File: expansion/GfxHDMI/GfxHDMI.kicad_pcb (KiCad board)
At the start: 4 copper layers, 100 x 100 mm, 76 parts, among them J1 JTAG, J101 D68K_64PIN_BOARD, J501 VGA Out, U101 74LS125, U102 LD1117S12TR_SOT223, U201 SN74LVC8T245PWR, U202 SN74LVC8T245PWR, U203 SN74LVC8T245PWR, U204 SN74LVC8T245PWR, U205 SN74LVC8T245PWR, U206 SN74LVC8T245PWR, U301 XC3S500E-4PQG208I, U302 W25Q64JVSSIM, U401 IS61WV102416FBLL-10TLI, U402 IS61WV102416FBLL-10TLI, U501 ADV7123JSTZ240, Y1 ECS-3963

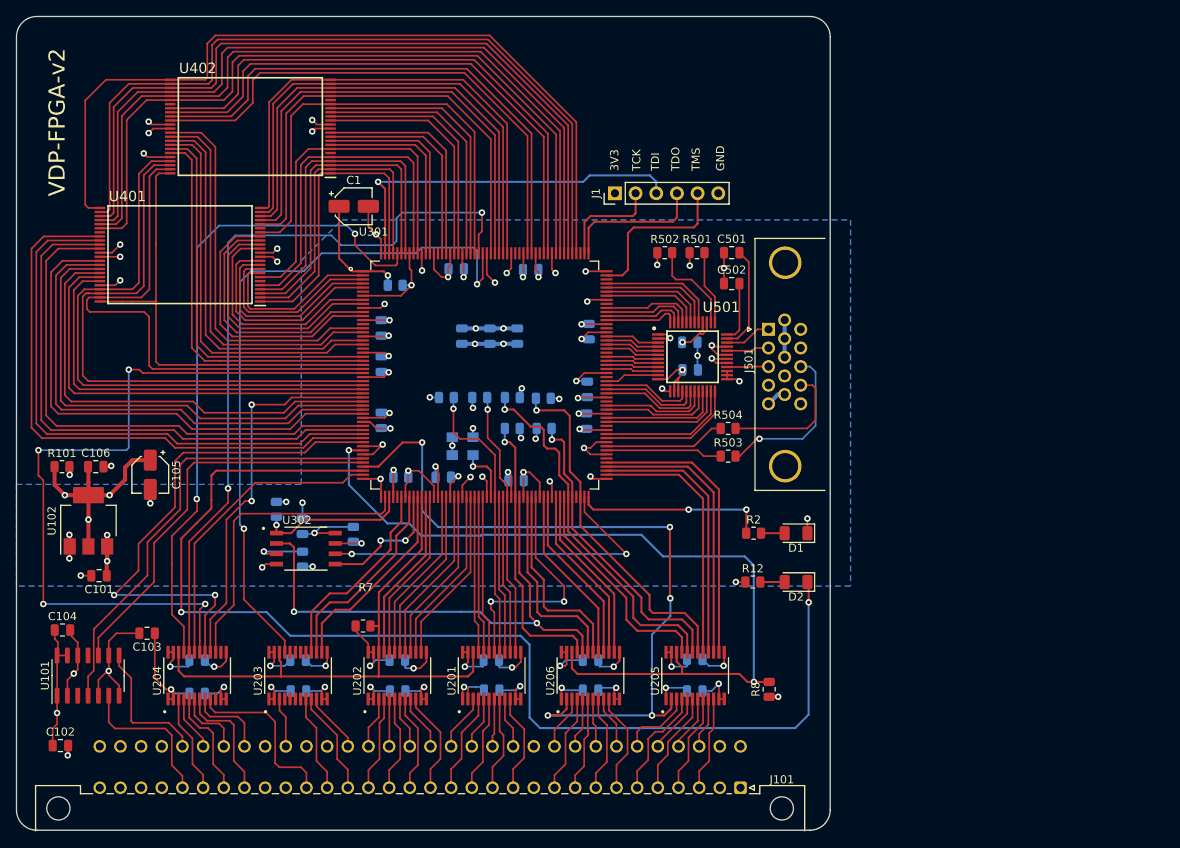
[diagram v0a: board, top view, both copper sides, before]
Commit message: Working on HDMI board
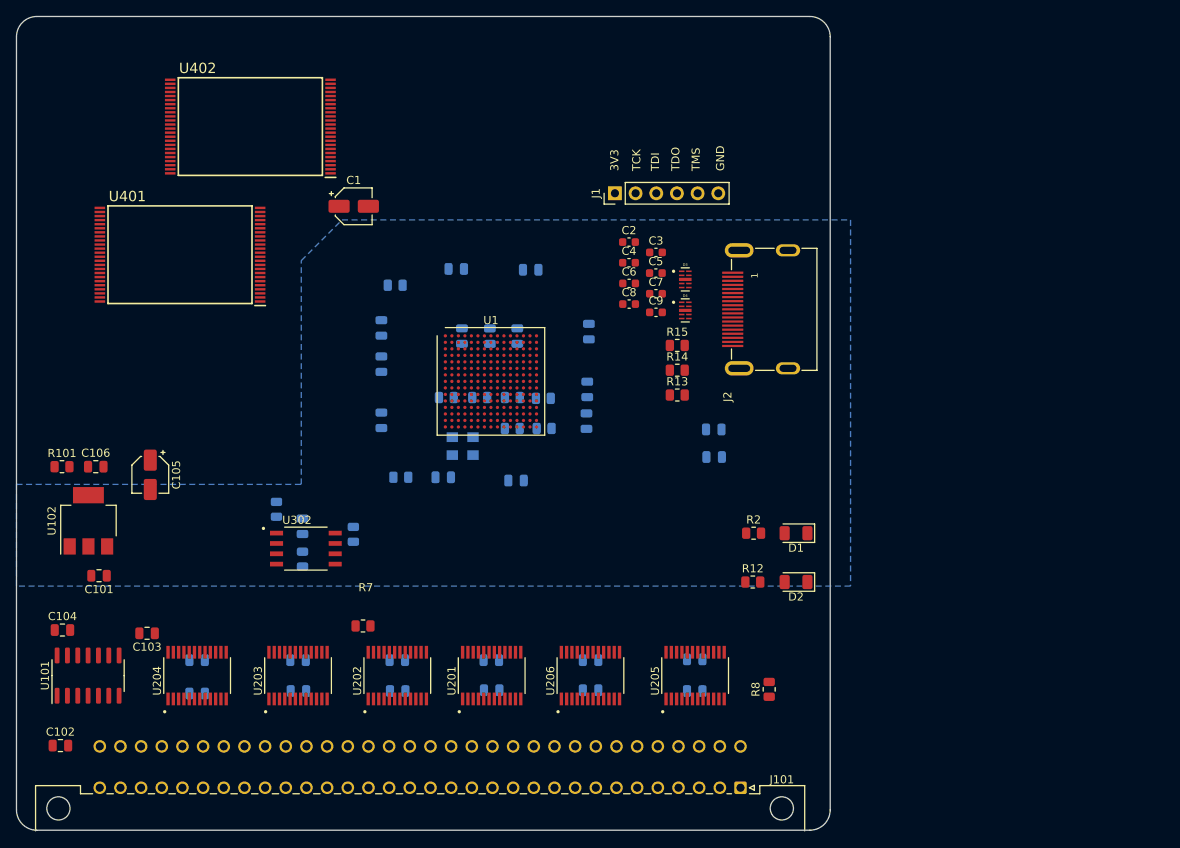
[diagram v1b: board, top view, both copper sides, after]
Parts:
- removed C501, C502: 100nF, Capacitor_SMD:C_0805_2012Metric
- removed J501: VGA Out, Connector_Dsub:DSUB-15-HD_Female_Horizontal_P2.29x1.98mm_EdgePinOffset3.03mm_Housed_MountingHolesOffset4.94mm
- removed R501: 530R, Resistor_SMD:R_0805_2012Metric
- removed R502: 10K, Resistor_SMD:R_0805_2012Metric
- removed R503, R504: 82.5R, Resistor_SMD:R_0805_2012Metric
- removed U301: XC3S500E-4PQG208I, Ddraig:QFP50P3060X3060X409-208N
- removed U501: ADV7123JSTZ240, Ddraig:QFP50P900X900X160-48N
- added C2: 100nF, Capacitor_SMD:C_0603_1608Metric, F.Cu at (175.3, 77.7)
- added C3: 100nF, Capacitor_SMD:C_0603_1608Metric, F.Cu at (178.6, 79.0)
- added C4: 100nF, Capacitor_SMD:C_0603_1608Metric, F.Cu at (175.3, 80.3)
- added C5: 100nF, Capacitor_SMD:C_0603_1608Metric, F.Cu at (178.6, 81.5)
- added C6: 100nF, Capacitor_SMD:C_0603_1608Metric, F.Cu at (175.3, 82.8)
- added C7: 100nF, Capacitor_SMD:C_0603_1608Metric, F.Cu at (178.6, 84.1)
- added C8: 100nF, Capacitor_SMD:C_0603_1608Metric, F.Cu at (175.3, 85.3)
- added C9: 100nF, Capacitor_SMD:C_0603_1608Metric, F.Cu at (178.6, 86.4)
- added D3: RCLAMP0524PATCT, Ddraig:DIO_RCLAMP0524PATCT, F.Cu at (182.2, 82.3)
- added D4: RCLAMP0524PATCT, Ddraig:DIO_RCLAMP0524PATCT, F.Cu at (182.2, 86.1)
- added J2: 685119134923, Ddraig:685119134923, F.Cu at (188.0, 86.0)
- added R13: 10K, Resistor_SMD:R_0805_2012Metric, F.Cu at (181.2, 96.5)
- added R14: 10K, Resistor_SMD:R_0805_2012Metric, F.Cu at (181.2, 93.5)
- added R15: 10K, Resistor_SMD:R_0805_2012Metric, F.Cu at (181.2, 90.4)
- added U1: XC7S25-CSGA225, Package_BGA:Xilinx_CSGA225, F.Cu at (158.3, 94.8)
- U302: value W25Q64JVSSIM -> IS25LP064D-JBLE
- moved C503 11.1 mm to (185.7, 100.8)
- moved C504 11.1 mm to (185.7, 104.1)
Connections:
- C307 pad 2: GND -> Net-(C307-Pad2)
- C308 pad 2: GND -> Net-(C307-Pad2)
- C309 pad 2: GND -> Net-(C307-Pad2)
- C310 pad 2: GND -> Net-(C307-Pad2)
- J1 pad 2: Net-(J1-Pad2) -> unconnected-(J1-Pin_2-Pad2)
- J1 pad 3: Net-(J1-Pad3) -> unconnected-(J1-Pin_3-Pad3)
- J1 pad 4: Net-(J1-Pad4) -> unconnected-(J1-Pin_4-Pad4)
- J1 pad 5: Net-(J1-Pad5) -> unconnected-(J1-Pin_5-Pad5)
- U302 pad 2: /FPGA/D14 -> /FPGA/FLASH_DO
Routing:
- net GND: track 230.9 -> 0.00 mm, vias 61 -> 0
- net +3V3: track 170.2 -> 0.00 mm, vias 42 -> 0
- net /FPGA/~{ACCESS_LED}: track 142.5 -> 0.00 mm, vias 2 -> 0
- net /FPGA/~{CPU_DATAEN}: track 104.1 -> 0.00 mm, vias 2 -> 0
- net /FPGA/SRAM_A14: track 101.4 -> 0.00 mm
- net /FPGA/SRAM_A13: track 97.3 -> 0.00 mm
- net /FPGA/SRAM_A12: track 96.3 -> 0.00 mm
- net /FPGA/SRAM_A11: track 95.1 -> 0.00 mm
- net /FPGA/~{RESET}: track 95.0 -> 0.00 mm, vias 4 -> 0
- net /FPGA/SRAM_A10: track 93.9 -> 0.00 mm
- net /FPGA/SRAM_A9: track 93.0 -> 0.00 mm
- net /FPGA/~{DATACS}: track 92.8 -> 0.00 mm, vias 2 -> 0
- net /FPGA/DATA_DIR: track 92.8 -> 0.00 mm, vias 5 -> 0
- net /FPGA/HOST_CLK: track 87.0 -> 0.00 mm, vias 2 -> 0
- net /FPGA/~{REGCS}: track 81.6 -> 0.00 mm, vias 2 -> 0
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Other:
- board text removed: "VDP-FPGA-v2"

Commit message: More work on the HDMI board
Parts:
- R13: value 10K -> 27K
- R14, R15: value 10K -> 1K5
- moved C305 62.4 mm to (220.6, 89.0)
- moved C307 62.4 mm to (225.6, 80.8)
- moved C310 62.4 mm to (214.9, 106.3)
- moved R9 62.4 mm to (223.4, 96.5)
- moved C301 62.4 mm to (224.0, 89.0)
- moved C302 62.4 mm to (232.6, 95.5)
- moved C303 62.4 mm to (217.2, 89.0)
- moved C304 62.4 mm to (207.3, 99.3)
- moved C306 62.4 mm to (232.8, 88.4)
- moved C308 62.4 mm to (232.5, 99.4)
- moved C309 62.4 mm to (207.3, 88.0)
- moved C401 62.4 mm to (223.8, 106.7)
- moved C402 62.4 mm to (207.3, 92.4)
- moved C404 62.4 mm to (216.5, 80.7)
- moved R1 62.4 mm to (219.4, 96.5)
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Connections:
- C307 pad 2: Net-(C307-Pad2) -> GND
- C308 pad 2: Net-(C307-Pad2) -> GND
- C309 pad 2: Net-(C307-Pad2) -> GND
- C310 pad 2: Net-(C307-Pad2) -> GND
- J2 pad 18: unconnected-(J2-+5V-Pad18) -> +5V
- U1 pad A1: unconnected-(U1E-GND-PadA1) -> GND
- U1 pad A15: unconnected-(U1E-GND-PadA15) -> GND
- U1 pad B15: unconnected-(U1C-IO_L14N_T2_SRCC_15-PadB15) -> /VGA/HDMI_TX2_N
- U1 pad B7: unconnected-(U1C-VCCO_15-PadB7) -> +3V3
- U1 pad B8: unconnected-(U1E-GND-PadB8) -> GND
- U1 pad C11: unconnected-(U1C-VCCO_15-PadC11) -> +3V3
- U1 pad C12: unconnected-(U1E-GND-PadC12) -> GND
- U1 pad C15: unconnected-(U1C-IO_L14P_T2_SRCC_15-PadC15) -> /VGA/HDMI_TX2_P
- U1 pad C2: unconnected-(U1E-GND-PadC2) -> GND
- U1 pad C3: unconnected-(U1D-VCCO_34-PadC3) -> +3V3
- U1 pad D14: unconnected-(U1E-GND-PadD14) -> GND
- U1 pad D15: unconnected-(U1C-IO_L19N_T3_VREF_15-PadD15) -> /VGA/HDMI_TX1_N
- U1 pad D5: unconnected-(U1A-VCCBATT_0-PadD5) -> +3V3
- U1 pad D6: unconnected-(U1E-GND-PadD6) -> GND
- U1 pad E10: unconnected-(U1E-VCCINT-PadE10) -> +3V3
- U1 pad E14: unconnected-(U1C-IO_L19P_T3_15-PadE14) -> /VGA/HDMI_TX1_P
- U1 pad E15: unconnected-(U1C-IO_L21N_T3_DQS_15-PadE15) -> /VGA/HDMI_TX0_N
- U1 pad E4: unconnected-(U1E-GND-PadE4) -> GND
- U1 pad E6: unconnected-(U1A-VCCO_0-PadE6) -> +3V3
- U1 pad E7: unconnected-(U1E-GND-PadE7) -> GND
- U1 pad E8: unconnected-(U1E-VCCINT-PadE8) -> +3V3
- U1 pad E9: unconnected-(U1E-GND-PadE9) -> GND
- U1 pad F10: unconnected-(U1E-GND-PadF10) -> GND
- U1 pad F12: unconnected-(U1C-VCCO_15-PadF12) -> +3V3
- U1 pad F13: unconnected-(U1E-GND-PadF13) -> GND
- U1 pad F14: unconnected-(U1C-IO_L21P_T3_DQS_15-PadF14) -> /VGA/HDMI_TX0_P
- U1 pad F15: unconnected-(U1C-IO_L20N_T3_15-PadF15) -> /VGA/HDMI_TXC_N
- U1 pad F6: unconnected-(U1E-GND-PadF6) -> GND
- U1 pad F7: unconnected-(U1E-VCCINT-PadF7) -> +3V3
- U1 pad F8: unconnected-(U1A-GNDADC_0-PadF8) -> GND
- U1 pad F9: unconnected-(U1A-VCCADC_0-PadF9) -> +3V3
- U1 pad G10: unconnected-(U1E-VCCINT-PadG10) -> +3V3
- U1 pad G15: unconnected-(U1C-IO_L20P_T3_15-PadG15) -> /VGA/HDMI_TXC_P
- U1 pad G2: unconnected-(U1D-VCCO_34-PadG2) -> +3V3
- U1 pad G3: unconnected-(U1E-GND-PadG3) -> GND
- U1 pad G6: unconnected-(U1E-VCCBRAM-PadG6) -> +3V3
- U1 pad G7: unconnected-(U1E-GND-PadG7) -> GND
- U1 pad G8: unconnected-(U1A-VREFN_0-PadG8) -> +3V3
- U1 pad H10: unconnected-(U1E-GND-PadH10) -> GND
- U1 pad H6: unconnected-(U1E-GND-PadH6) -> GND
- U1 pad H7: unconnected-(U1E-VCCINT-PadH7) -> +3V3
- U1 pad H9: unconnected-(U1A-VREFP_0-PadH9) -> +3V3
- U1 pad J10: unconnected-(U1E-VCCINT-PadJ10) -> +3V3
- U1 pad J13: unconnected-(U1E-GND-PadJ13) -> GND
- U1 pad J14: unconnected-(U1B-VCCO_14-PadJ14) -> +3V3
- U1 pad J6: unconnected-(U1E-VCCBRAM-PadJ6) -> +3V3
- U1 pad J7: unconnected-(U1E-GND-PadJ7) -> GND
- U1 pad K10: unconnected-(U1E-GND-PadK10) -> GND
- U1 pad K6: unconnected-(U1E-GND-PadK6) -> GND
- U1 pad K7: unconnected-(U1E-VCCINT-PadK7) -> +3V3
- U1 pad K8: unconnected-(U1E-GND-PadK8) -> GND
- U1 pad K9: unconnected-(U1E-VCCINT-PadK9) -> +3V3
- U1 pad L2: unconnected-(U1E-GND-PadL2) -> GND
- U1 pad L3: unconnected-(U1D-VCCO_34-PadL3) -> +3V3
- U1 pad L6: unconnected-(U1E-VCCAUX-PadL6) -> +3V3
- U1 pad L7: unconnected-(U1E-GND-PadL7) -> GND
- U1 pad L8: unconnected-(U1E-VCCAUX-PadL8) -> +3V3
- U1 pad L9: unconnected-(U1E-GND-PadL9) -> GND
- U1 pad M11: unconnected-(U1E-GND-PadM11) -> GND
- U1 pad M12: unconnected-(U1B-VCCO_14-PadM12) -> +3V3
- U1 pad P13: unconnected-(U1E-GND-PadP13) -> GND
- U1 pad P4: unconnected-(U1E-GND-PadP4) -> GND
- U1 pad P5: unconnected-(U1A-VCCO_0-PadP5) -> +3V3
- U1 pad P8: unconnected-(U1E-GND-PadP8) -> GND
- U1 pad P9: unconnected-(U1B-VCCO_14-PadP9) -> +3V3
- U1 pad R1: unconnected-(U1E-GND-PadR1) -> GND
- U1 pad R15: unconnected-(U1E-GND-PadR15) -> GND

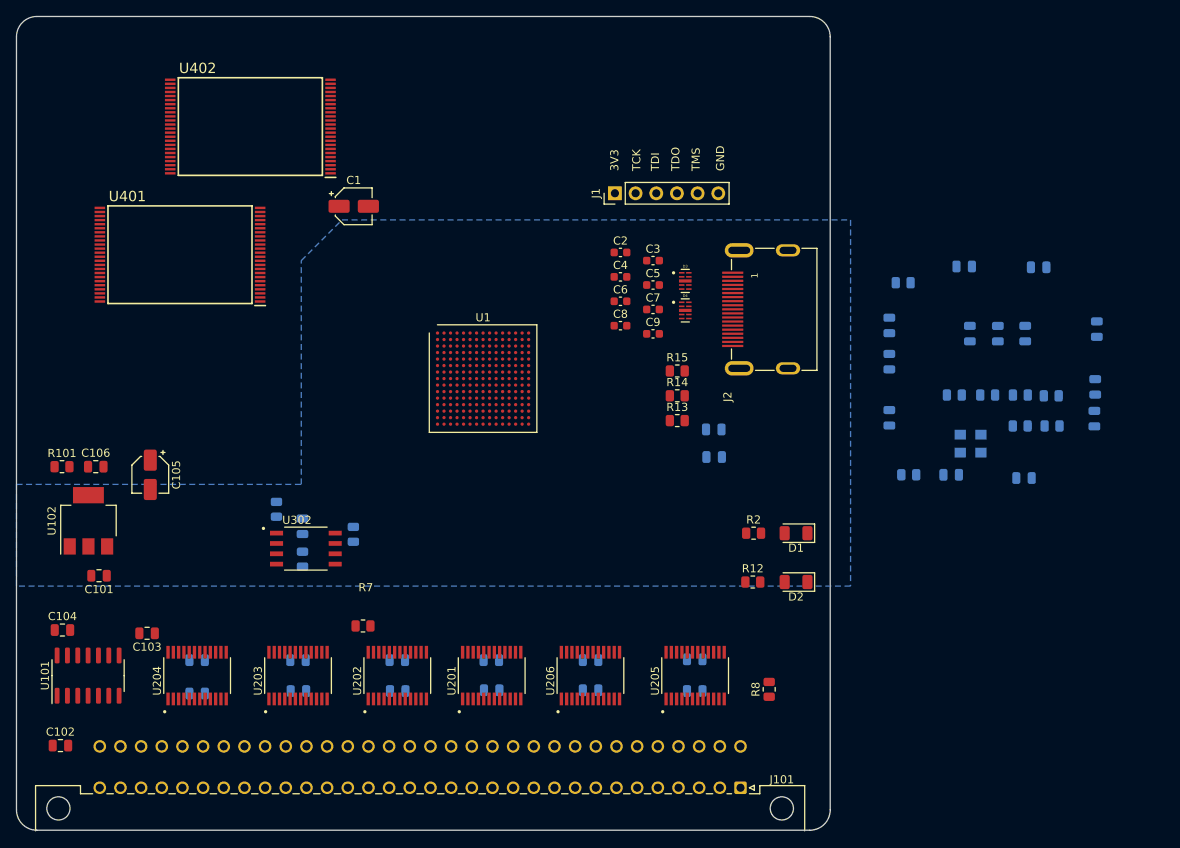
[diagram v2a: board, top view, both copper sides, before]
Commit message: Added HDMI card based on VGA design
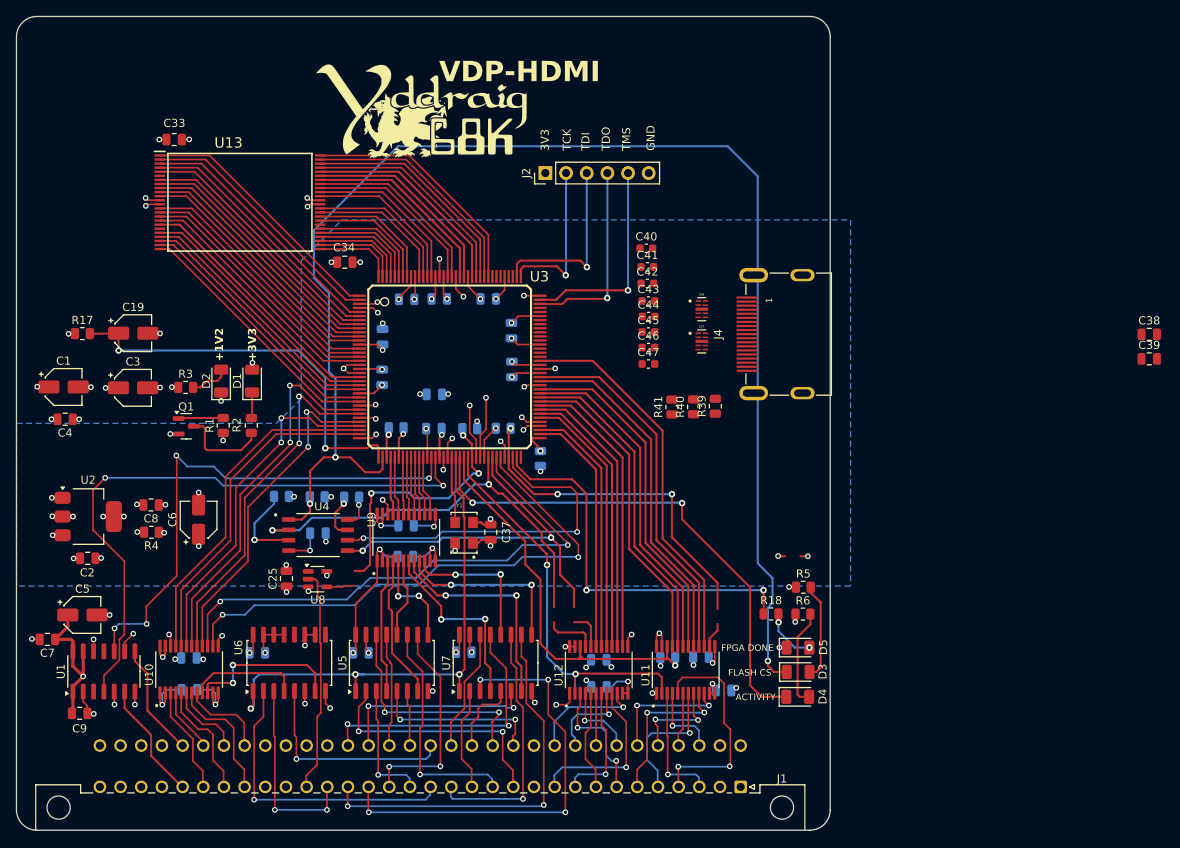
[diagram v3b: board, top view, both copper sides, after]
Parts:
- removed C101, C102, C103, C104, C106, C201, C202, C203, C204, C205, C206, C207, C208, C209, C210, C211, C212, C301, C302, C303, C304, C305, C306, C307, C308, C309, C310, C401, C402, C403, C404, C503, C504: 100nF, Capacitor_SMD:C_0805_2012Metric
- removed C105: 10uF, Capacitor_SMD:CP_Elec_4x5.3
- removed the J2 at (188.0, 86.0)
- removed R10, R11, R301, R302, R303: 10K, Resistor_SMD:R_0805_2012Metric
- removed R101: 120R, Resistor_SMD:R_0805_2012Metric
- removed R12: 390R, Resistor_SMD:R_0805_2012Metric
- removed R13: 27K, Resistor_SMD:R_0805_2012Metric
- removed U101: 74LS125, Package_SO:SO-14_3.9x8.65mm_P1.27mm
- removed U102: LD1117S12TR_SOT223, Package_TO_SOT_SMD:SOT-223-3_TabPin2
- removed U201, U202, U203, U204, U205, U206: SN74LVC8T245PWR, Ddraig:SOP65P640X120-24N
- removed U302: IS25LP064D-JBLE, Ddraig:SOIC127P790X195-8N
- removed U401, U402: IS61WV102416FBLL-10TLI, Ddraig:SOP50P2000X120-48N
- added C10: 100nF, Capacitor_SMD:C_0805_2012Metric, B.Cu at (144.9, 94.3)
- added C11: 100nF, Capacitor_SMD:C_0805_2012Metric, B.Cu at (151.3, 100.7)
- added C12: 100nF, Capacitor_SMD:C_0805_2012Metric, B.Cu at (160.9, 93.4)
- added C13: 100nF, Capacitor_SMD:C_0805_2012Metric, B.Cu at (152.0, 84.7)
- added C14: 100nF, Capacitor_SMD:C_0805_2012Metric, B.Cu at (137.1, 113.5)
- added C15: 100nF, Capacitor_SMD:C_0805_2012Metric, B.Cu at (151.3, 96.4)
- added C16: 100nF, Capacitor_SMD:C_0805_2012Metric, B.Cu at (145.0, 89.4)
- added C17: 100nF, Capacitor_SMD:C_0805_2012Metric, B.Cu at (160.8, 88.6)
- added C18: 100nF, Capacitor_SMD:C_0805_2012Metric, B.Cu at (147.9, 84.8)
- added C19: 0.1uF, Capacitor_SMD:CP_Elec_4x5.3, F.Cu at (114.3, 88.9)
- added C20: 100nF, Capacitor_SMD:C_0805_2012Metric, B.Cu at (158.0, 84.7)
- added C21: 100nF, Capacitor_SMD:C_0805_2012Metric, B.Cu at (184.1, 128.7)
- added C22: 100nF, Capacitor_SMD:C_0805_2012Metric, B.Cu at (171.6, 129.1)
- added C23: 100nF, Capacitor_SMD:C_0805_2012Metric, B.Cu at (147.9, 112.6)
- added C24: 100nF, Capacitor_SMD:C_0805_2012Metric, B.Cu at (121.2, 128.8)
- added C25: 100nF, Capacitor_SMD:C_0805_2012Metric, F.Cu at (133.2, 119.1)
- added C26: 100nF, Capacitor_SMD:C_0805_2012Metric, B.Cu at (186.9, 132.8)
- added C27: 100nF, Capacitor_SMD:C_0805_2012Metric, B.Cu at (171.6, 132.4)
- added C28: 100nF, Capacitor_SMD:C_0805_2012Metric, B.Cu at (155.0, 128.1)
- added C29: 100nF, Capacitor_SMD:C_0805_2012Metric, B.Cu at (142.3, 128.2)
- added C30: 100nF, Capacitor_SMD:C_0805_2012Metric, B.Cu at (129.6, 128.2)
- added C31: 100nF, Capacitor_SMD:C_0805_2012Metric, B.Cu at (121.2, 132.7)
- added C32: 100nF, Capacitor_SMD:C_0805_2012Metric, B.Cu at (147.8, 116.4)
- added C33: 100nF, Capacitor_SMD:C_0805_2012Metric, F.Cu at (119.4, 65.1)
- added C34: 100nF, Capacitor_SMD:C_0805_2012Metric, F.Cu at (140.3, 80.2)
- added C37: 100nF, Capacitor_SMD:C_0805_2012Metric, F.Cu at (158.3, 113.4)
- added C38: 100nF, Capacitor_SMD:C_0805_2012Metric, F.Cu at (239.2, 89.1)
- added C39: 100nF, Capacitor_SMD:C_0805_2012Metric, F.Cu at (239.2, 92.1)
- added C40: 100nF, Capacitor_SMD:C_0603_1608Metric, F.Cu at (177.4, 78.5)
- added C41: 100nF, Capacitor_SMD:C_0603_1608Metric, F.Cu at (177.5, 80.8)
- added C42: 100nF, Capacitor_SMD:C_0603_1608Metric, F.Cu at (177.5, 82.8)
- added C43: 100nF, Capacitor_SMD:C_0603_1608Metric, F.Cu at (177.7, 85.0)
- added C44: 100nF, Capacitor_SMD:C_0603_1608Metric, F.Cu at (177.7, 86.9)
- added C45: 100nF, Capacitor_SMD:C_0603_1608Metric, F.Cu at (177.7, 88.8)
- added C46: 100nF, Capacitor_SMD:C_0603_1608Metric, F.Cu at (177.7, 90.7)
- added C47: 100nF, Capacitor_SMD:C_0603_1608Metric, F.Cu at (177.7, 92.7)
- added D5: LED, LED_SMD:LED_1206_3216Metric, F.Cu at (196.0, 127.6)
- added D6: RCLAMP0524PATCT, Ddraig:DIO_RCLAMP0524PATCT, F.Cu at (184.2, 86.0)
- added D7: RCLAMP0524PATCT, Ddraig:DIO_RCLAMP0524PATCT, F.Cu at (184.2, 89.9)
- added J4: 685119134923, Ddraig:685119134923, F.Cu at (189.8, 89.0)
- added Q1: BC847, Package_TO_SOT_SMD:SOT-23, F.Cu at (120.9, 100.4)
- added R16: 10K, Resistor_SMD:R_0805_2012Metric, B.Cu at (146.7, 100.6)
- added R17: 10K, Resistor_SMD:R_0805_2012Metric, F.Cu at (108.1, 89.0)
- added R18: 390R, Resistor_SMD:R_0805_2012Metric, F.Cu at (192.7, 123.4)
- added R19: 10K, Resistor_SMD:R_0805_2012Metric, B.Cu at (164.4, 104.3)
- added R20: 10K, Resistor_SMD:R_0805_2012Metric, B.Cu at (180.0, 128.8)
- added R39: 27K, Resistor_SMD:R_0805_2012Metric, F.Cu at (185.9, 97.9)
- added R40: 1K5, Resistor_SMD:R_0805_2012Metric, F.Cu at (183.2, 98.0)
- added R41: 1K5, Resistor_SMD:R_0805_2012Metric, F.Cu at (180.5, 98.0)
- added U10: SN74LVC8T245PWR, Ddraig:SOP65P640X120-24N, F.Cu at (121.2, 130.3)
- added U11: SN74LVC8T245PWR, Ddraig:SOP65P640X120-24N, F.Cu at (182.2, 130.3)
- added U12: SN74LVC8T245PWR, Ddraig:SOP65P640X120-24N, F.Cu at (171.6, 130.3)
- added U13: IS61WV102416FBLL-10TLI, Ddraig:SOP50P2000X120-48N, F.Cu at (127.5, 72.8)
- added U2: LD1117S12TR_SOT223, Package_TO_SOT_SMD:SOT-223-3_TabPin2, F.Cu at (108.8, 111.5)
- added U3: XC6SLX9-TQG144, Ddraig:TQ144, F.Cu at (153.2, 93.1)
- added U4: W25Q64JVSSIM, Ddraig:SOIC127P790X195-8N, F.Cu at (137.1, 113.7)
- added U5: SN74LS157NSR, Package_SO:SO-16_5.3x10.2mm_P1.27mm, F.Cu at (146.1, 129.4)
- added U6: SN74LS157NSR, Package_SO:SO-16_5.3x10.2mm_P1.27mm, F.Cu at (133.5, 129.4)
- added U7: SN74LS157NSR, Package_SO:SO-16_5.3x10.2mm_P1.27mm, F.Cu at (158.9, 129.4)
- added U8: SN74LV1T34DBV, Package_TO_SOT_SMD:SOT-23-5, F.Cu at (137.0, 119.2)
- added U9: SN74LVC8T245PWR, Ddraig:SOP65P640X120-24N, F.Cu at (147.9, 114.0)
- added Z1: ~, Ddraig:Ddraig68k-26mm, F.Cu at (149.9, 61.4)
- C1: value 0.1uF -> 47uF
- C2, C4, C7, C8, C9: footprint Capacitor_SMD:C_0603_1608Metric -> Capacitor_SMD:C_0805_2012Metric
- C3, C5: value 100nF -> 47uF; footprint Capacitor_SMD:C_0603_1608Metric -> Capacitor_SMD:CP_Elec_4x5.3
- C6: value 100nF -> 10uF; footprint Capacitor_SMD:C_0603_1608Metric -> Capacitor_SMD:CP_Elec_4x5.3
- D3, D4: value RCLAMP0524PATCT -> LED; footprint Ddraig:DIO_RCLAMP0524PATCT -> LED_SMD:LED_1206_3216Metric
- R1, R3, Y1: moved to F.Cu
- R14, R15: value 1K5 -> 10K; moved to B.Cu
- R4: value 10K -> 120R; moved to F.Cu
- R5, R6: value 10K -> 390R; moved to F.Cu
- R7, R8: moved to B.Cu
- U1: value XC7S25-CSGA225 -> SN74LS125ADR; footprint Package_BGA:Xilinx_CSGA225 -> Package_SO:SO-14_3.9x8.65mm_P1.27mm
- moved R4 107.6 mm to (116.6, 113.4)
- moved R3 94.5 mm to (120.8, 95.6), turned to 0 degrees
- moved R1 94.0 mm to (125.4, 100.3), turned to 90 degrees
- moved C7 84.8 mm to (103.8, 126.5), turned to 180 degrees
- moved C9 84.5 mm to (107.8, 135.6)
- moved R9 83.1 mm to (141.2, 109.1)
- moved C5 81.0 mm to (108.1, 123.5)
- moved C2 75.5 mm to (108.8, 116.6)
- moved D2 74.8 mm to (125.2, 94.8), turned to 90 degrees
- moved C4 70.5 mm to (106.0, 99.5), turned to 180 degrees
- moved D1 69.4 mm to (129.0, 94.8), turned to 90 degrees
- moved C3 65.8 mm to (114.3, 95.6)
- moved Y1 63.2 mm to (155.0, 113.4), turned to 90 degrees
- moved R2 63.1 mm to (128.9, 100.3), turned to -90 degrees
- moved C8 61.8 mm to (116.5, 110.0), turned to 180 degrees
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- renumbered J101 to J1, J1 to J2
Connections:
- C1 pad 1: /FPGA/FPGA_PROGB -> +3V3
- C2 pad 1: /VGA/HDMI_TX2_P -> +3V3
- C2 pad 2: Net-(C2-Pad2) -> GND
- C3 pad 1: /VGA/HDMI_TX2_N -> +3V3
- C3 pad 2: Net-(C3-Pad2) -> GND
- C4 pad 1: /VGA/HDMI_TX1_P -> +3V3
- C4 pad 2: Net-(C4-Pad2) -> GND
- C5 pad 1: /VGA/HDMI_TX1_N -> +5V
- C5 pad 2: Net-(C5-Pad2) -> GND
- C6 pad 1: /VGA/HDMI_TX0_P -> +1V2
- C6 pad 2: Net-(C6-Pad2) -> GND
- C7 pad 1: /VGA/HDMI_TX0_N -> +5V
- C7 pad 2: Net-(C7-Pad2) -> GND
- C8 pad 1: /VGA/HDMI_TXC_P -> +1V2
- C8 pad 2: Net-(C8-Pad2) -> GND
- C9 pad 1: /VGA/HDMI_TXC_N -> +5V
- C9 pad 2: Net-(C9-Pad2) -> GND
- D1 pad 1: GND -> Net-(D1-K)
- D1 pad 2: Net-(D1-A) -> +3V3
- D2 pad 1: /FPGA/~{ACCESS_LED} -> GND
- D3 pad 1: Net-(C2-Pad2) -> /FPGA/~{FLASH_CS}
- D3 pad 2: Net-(C3-Pad2) -> Net-(D3-A)
- D4 pad 1: Net-(C6-Pad2) -> /FPGA/~{LED1}
- D4 pad 2: Net-(C7-Pad2) -> Net-(D4-A)
- J1 pad A28: Net-(J101-~{IRQ}) -> Net-(J1-~{IRQ})
- J1 pad C23: /CPU_CLK -> unconnected-(J1-SYS_CLK-PadC23)
- J1 pad C28: Net-(J101-~{ACK}) -> Net-(J1-~{ACK})
- J2 pad 2: unconnected-(J1-Pin_2-Pad2) -> /FPGA/TCK
- J2 pad 3: unconnected-(J1-Pin_3-Pad3) -> /FPGA/TDI
- J2 pad 4: unconnected-(J1-Pin_4-Pad4) -> /FPGA/TDO
- J2 pad 5: unconnected-(J1-Pin_5-Pad5) -> /FPGA/TMS
- R1 pad 1: /FPGA/A1 -> +1V2
- R1 pad 2: GND -> Net-(Q1-B)
- R14 pad 1: +5V -> +3V3
- R14 pad 2: Net-(J2-SCL) -> /FPGA/FPGA_M0
- R15 pad 1: +5V -> /FPGA/FPGA_M1
- R15 pad 2: Net-(J2-CEC) -> GND
- R2 pad 1: /FPGA/FPGA_DONE -> Net-(D1-K)
- R2 pad 2: Net-(D1-A) -> Net-(Q1-C)
- R3 pad 1: /FPGA/A4 -> +3V3
- R3 pad 2: GND -> Net-(D2-A)
- R4 pad 1: +3V3 -> +1V2
- R4 pad 2: /FPGA/D15 -> GND
- R5 pad 2: /FPGA/FPGA_INITB -> Net-(D3-A)
- R6 pad 2: /FPGA/FPGA_PROGB -> Net-(D4-A)
- R7 pad 2: /FPGA/~{BUSEN} -> Net-(U4-WP/IO2)
- R8 pad 2: /FPGA/~{CPU_DATAEN} -> /FPGA/~{FLASH_CS}
- R9 pad 2: /FPGA/D6 -> Net-(U4-HOLD/IO3)
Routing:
- net /FPGA/~{FLASH_CS}: track 0.00 -> 175.1 mm, vias 0 -> 3
- net GND: track 0.00 -> 138.2 mm, vias 0 -> 64
- net +3V3: track 0.00 -> 88.0 mm, vias 0 -> 48
- net /~{CPU_IRQ}: track 0.00 -> 75.3 mm, vias 0 -> 2
- net /FPGA/A9: track 0.00 -> 67.3 mm, vias 0 -> 2
- net /FPGA/A8: track 0.00 -> 66.1 mm, vias 0 -> 2
- net /~{CPU_DTACK}: track 0.00 -> 64.2 mm, vias 0 -> 4
- net /FPGA/ADDR_MUX: track 0.00 -> 64.0 mm, vias 0 -> 3
- net /FPGA/~{LED1}: track 0.00 -> 62.9 mm, vias 0 -> 2
- net /CPU_A15: track 0.00 -> 54.2 mm, vias 0 -> 4
- net /FPGA/FLASH_DO: track 0.00 -> 53.0 mm, vias 0 -> 2
- net +5V: track 0.00 -> 52.9 mm, vias 0 -> 10
- net /FPGA/~{CPU_DATAEN}: track 0.00 -> 50.9 mm, vias 0 -> 1
- net /FPGA/FPGA_PROGB: track 0.00 -> 49.1 mm, vias 0 -> 2
- net /CPU_A17: track 0.00 -> 48.6 mm, vias 0 -> 2
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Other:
- board text added: "+1V2"
- board text added: "+3V3"
- board text added: "ACTIVITY"
- board text added: "FLASH CS"
- board text added: "FPGA DONE"
- board text added: "VDP-HDMI"
